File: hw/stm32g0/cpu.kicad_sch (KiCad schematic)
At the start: 32 parts, among them J201 Conn_01x06, J202 Conn_01x04, J203 Conn_01x03, U201 STM32G030K8Tx, U202 74AHCT125, U203 CAT24C256

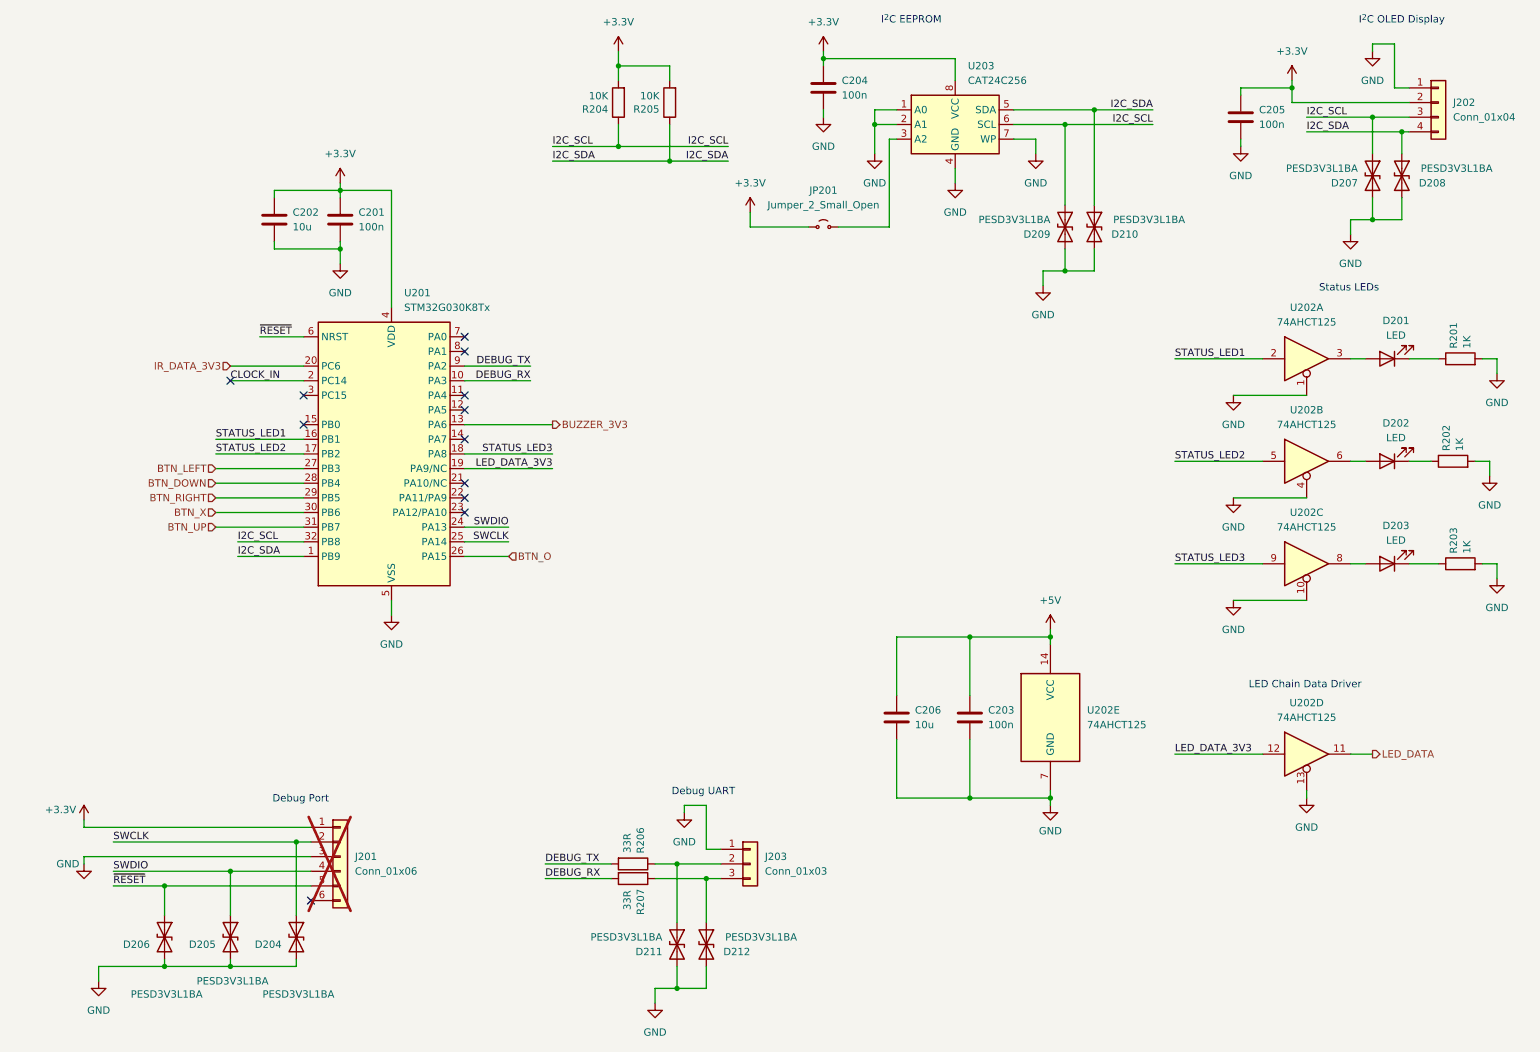
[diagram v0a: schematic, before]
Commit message: chore(hw): general improvements, utilize some unused CPU pins
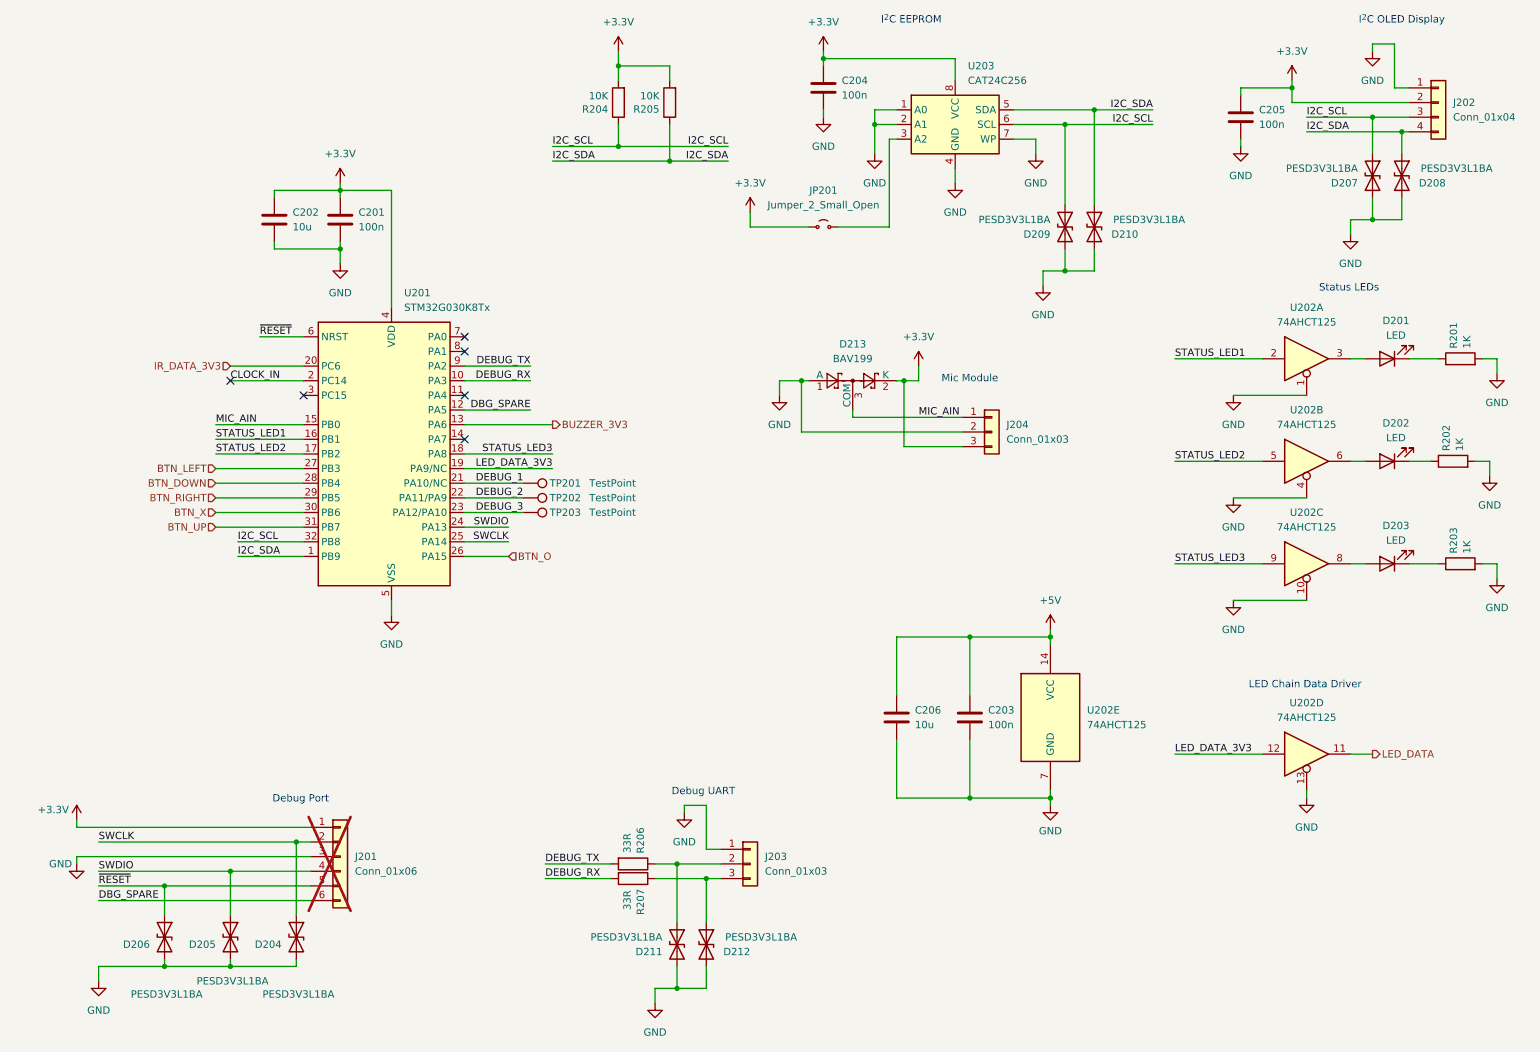
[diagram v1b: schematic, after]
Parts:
- added D213: BAV199, Package_TO_SOT_SMD:SOT-23_Handsoldering, symbol Diode:BAT54S
- added J204: Conn_01x03, Connector_PinHeader_2.54mm:PinHeader_1x03_P2.54mm_Vertical, symbol Connector_Generic:Conn_01x03
- added TP201, TP202, TP203: TestPoint, TestPoint:TestPoint_Pad_D1.0mm, symbol Connector:TestPoint
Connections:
- net +3.3V: now also D213.2 (K), J204.3 (Pin_3)
- net GND: now also D213.1 (A), J204.2 (Pin_2)
- net DBG_SPARE: now reaches U201.12 (PA5)
- net DBG_SPARE: now also J201.6 (Pin_6)
- net MIC_AIN: now reaches U201.15 (PB0)
- net MIC_AIN: now also D213.3 (COM), J204.1 (Pin_1)
- net DEBUG_1: now reaches U201.21 (PA10/NC)
- net DEBUG_1: now also TP201.1
- net DEBUG_2: now reaches U201.22 (PA11/PA9)
- net DEBUG_2: now also TP202.1
- net DEBUG_3: now reaches U201.23 (PA12/PA10)
- net DEBUG_3: now also TP203.1
- no-connect marks 12 -> 6
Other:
- note added: "Mic Module"

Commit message: chore(hw): move all signals to outer layers
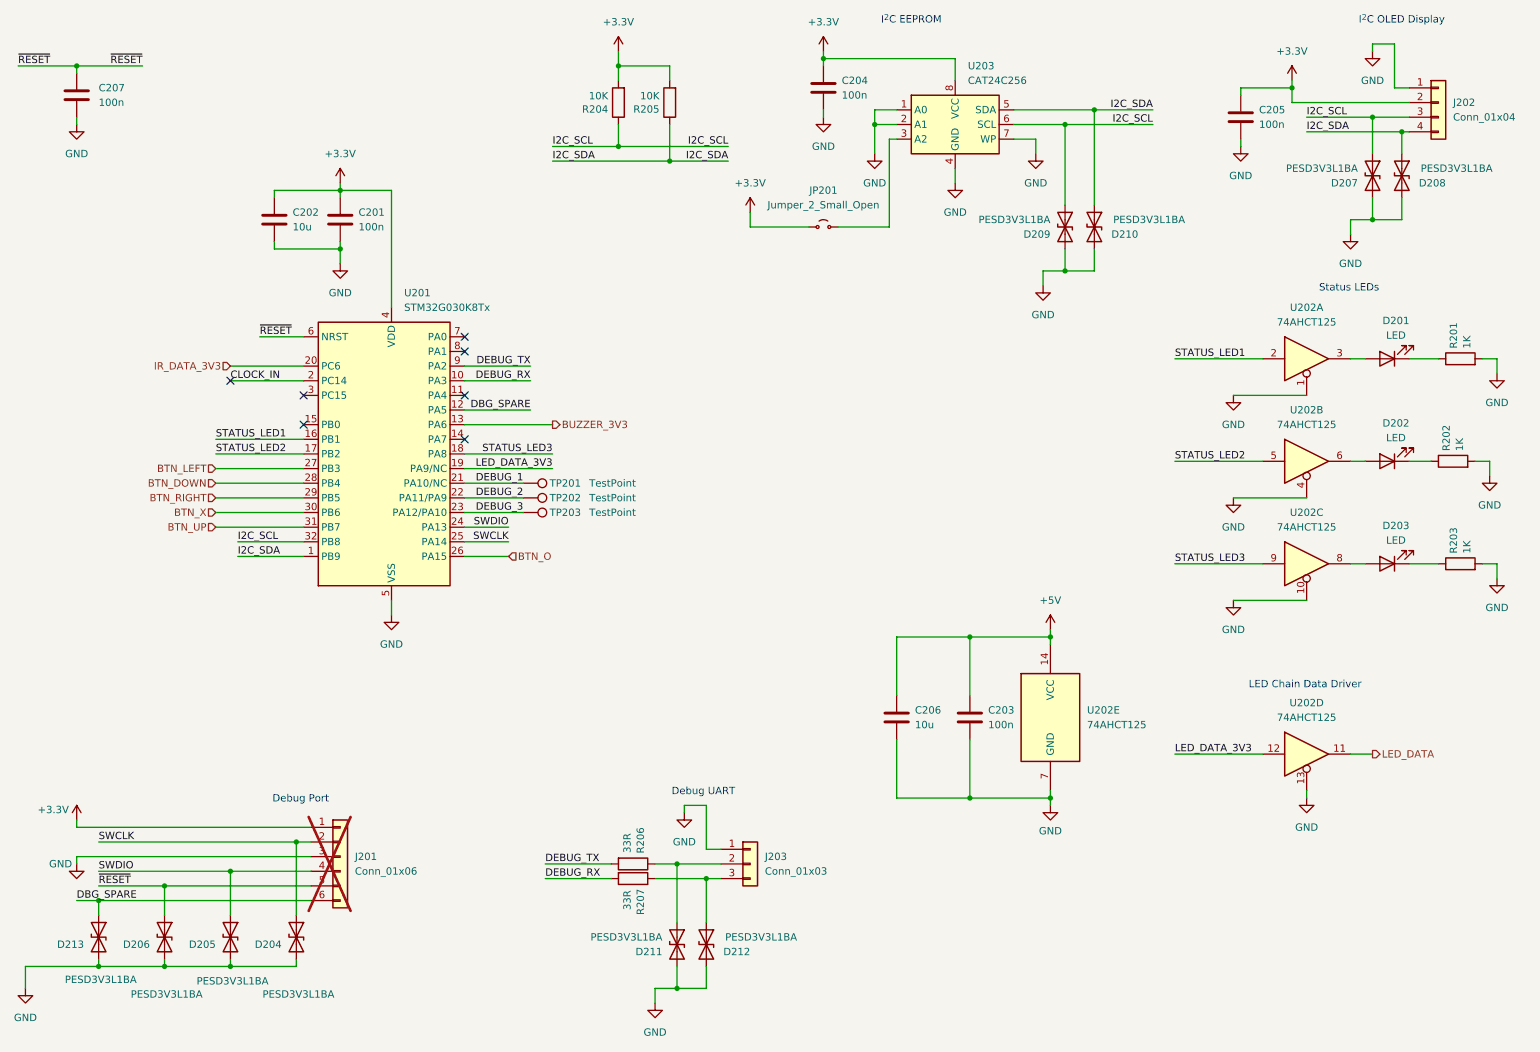
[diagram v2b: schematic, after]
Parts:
- removed D213: BAV199, Package_TO_SOT_SMD:SOT-23_Handsoldering, symbol Diode:BAT54S
- removed J204: Conn_01x03, Connector_PinHeader_2.54mm:PinHeader_1x03_P2.54mm_Vertical, symbol Connector_Generic:Conn_01x03
- added C207: 100n, Capacitor_SMD:C_0805_2012Metric_Pad1.18x1.45mm_HandSolder, symbol Device:C
- added D213: PESD3V3L1BA, Diode_SMD:D_SOD-323_HandSoldering, symbol Device:D_TVS
- TP201, TP202, TP203: footprint TestPoint:TestPoint_Pad_D1.0mm -> TestPoint:TestPoint_Pad_1.0x1.0mm
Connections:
- net DBG_SPARE: now also D213.1 (A1)
- net GND: now also C207.2, D213.2 (A2)
- net ~{RESET}: now also C207.1
- net MIC_AIN: no longer names the net of U201.15 (PB0)
- no-connect marks 6 -> 7
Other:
- note removed: "Mic Module"

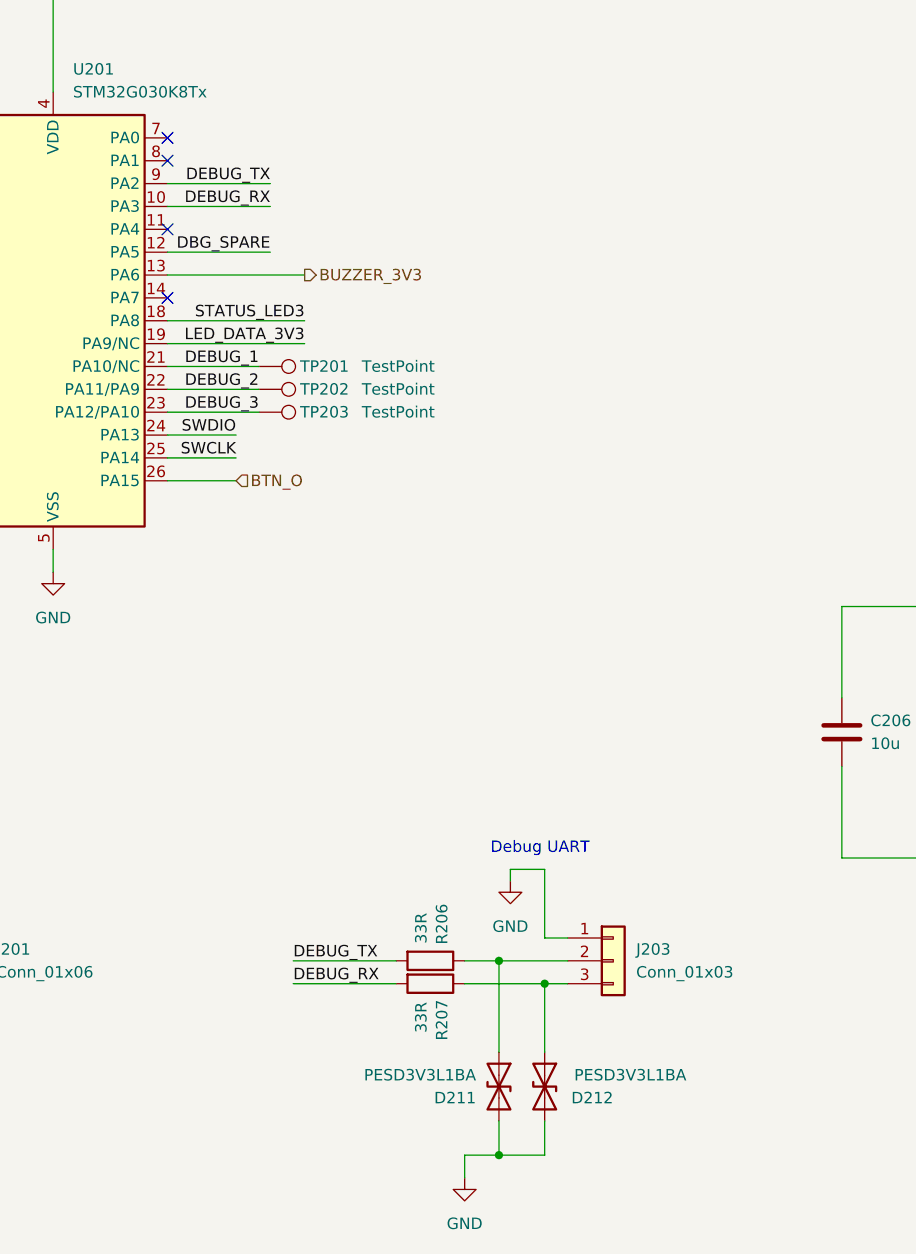
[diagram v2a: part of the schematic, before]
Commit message: chore(hw): add BT module supply and control pins
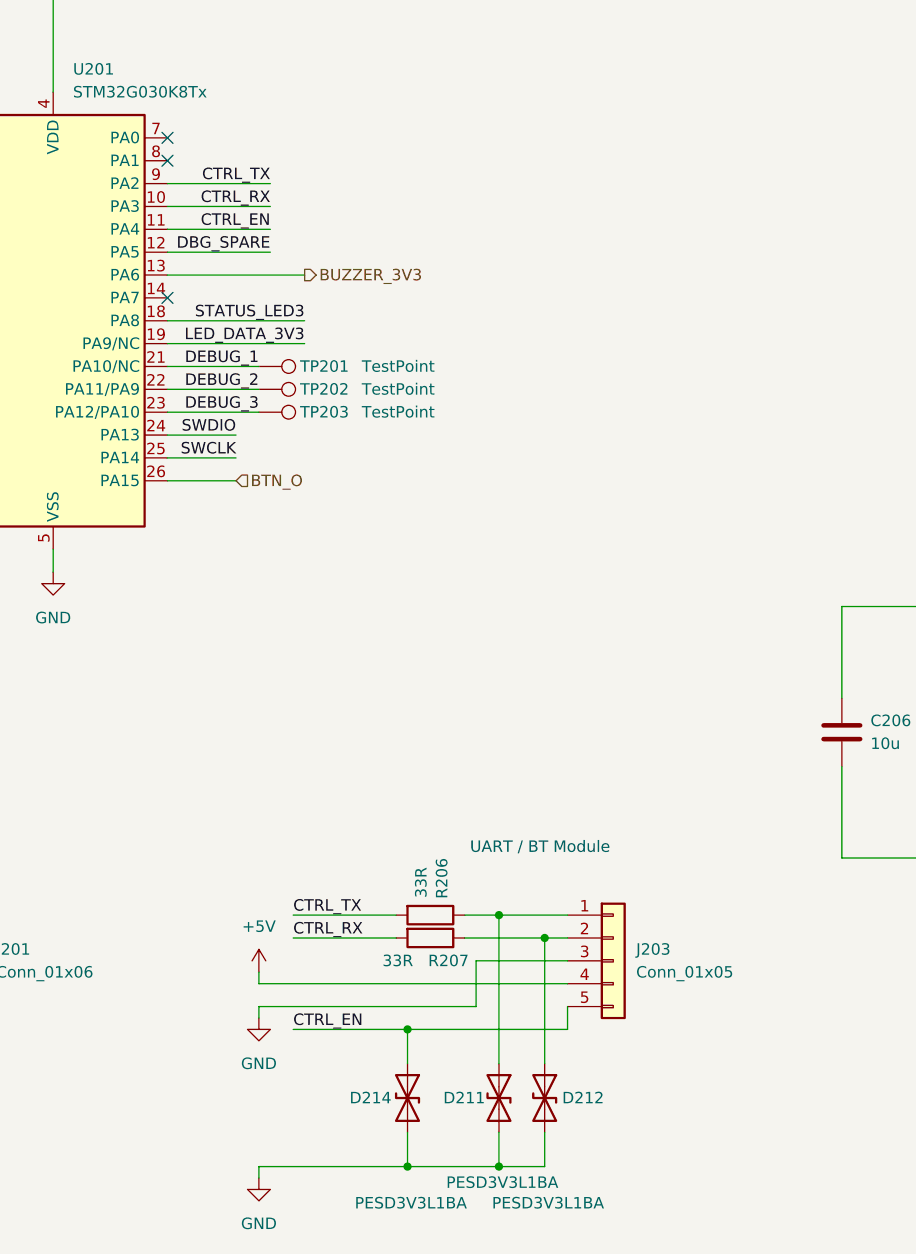
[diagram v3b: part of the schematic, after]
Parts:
- removed J203: Conn_01x03, Connector_PinHeader_2.54mm:PinHeader_1x03_P2.54mm_Vertical, symbol Connector_Generic:Conn_01x03
- added D214: PESD3V3L1BA, Diode_SMD:D_SOD-323_HandSoldering, symbol Device:D_TVS
- added J203: Conn_01x05, Connector_PinSocket_2.54mm:PinSocket_1x05_P2.54mm_Vertical, symbol Connector_Generic:Conn_01x05
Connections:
- net +5V: now also J203.4 (Pin_4)
- net GND: now also D214.2 (A2), J203.3 (Pin_3)
- net CTRL_EN: now reaches U201.11 (PA4)
- net CTRL_EN: now also D214.1 (A1), J203.5 (Pin_5)
- net at D212.1 (A1), R207.1: now also J203.2 (Pin_2)
- net at D211.1 (A1), R206.1: now also J203.1 (Pin_1)
- net DEBUG_RX renamed CTRL_RX
- net DEBUG_TX renamed CTRL_TX
- no-connect marks 7 -> 6
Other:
- note added: "UART / BT Module"
- note removed: "Debug UART"
- moved on the sheet: D211, D212, R206, R207

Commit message: chore(hw): change debug port to pin header
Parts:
- J201: footprint Connector_PinSocket_2.54mm:PinSocket_1x06_P2.54mm_Vertical -> Connector_PinHeader_2.54mm:PinHeader_1x06_P2.54mm_Vertical
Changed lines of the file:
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@@
 			)
 		)
-		(property "Footprint" "Connector_PinSocket_2.54mm:PinSocket_1x06_P2.54mm_Vertical"
+		(property "Footprint" "Connector_PinHeader_2.54mm:PinHeader_1x06_P2.54mm_Vertical"
 			(at 76.2 163.83 0)
 			(effects

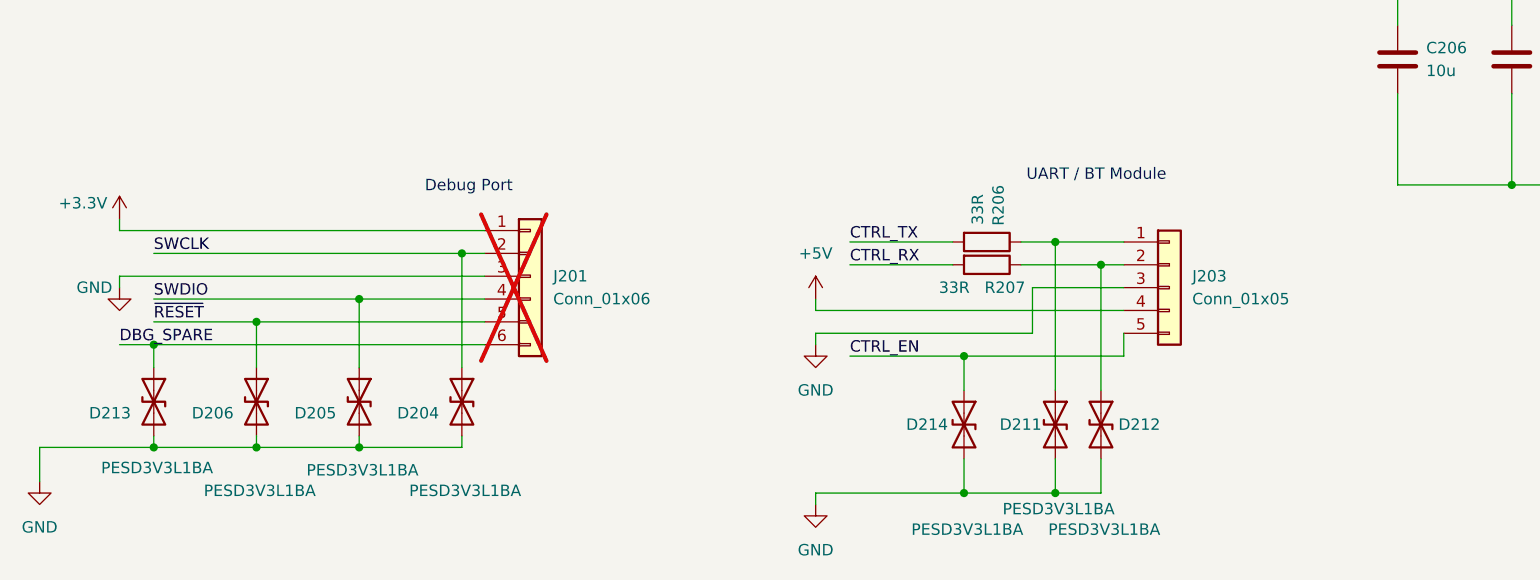
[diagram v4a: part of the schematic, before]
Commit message: chore(hw): add debug port resistors
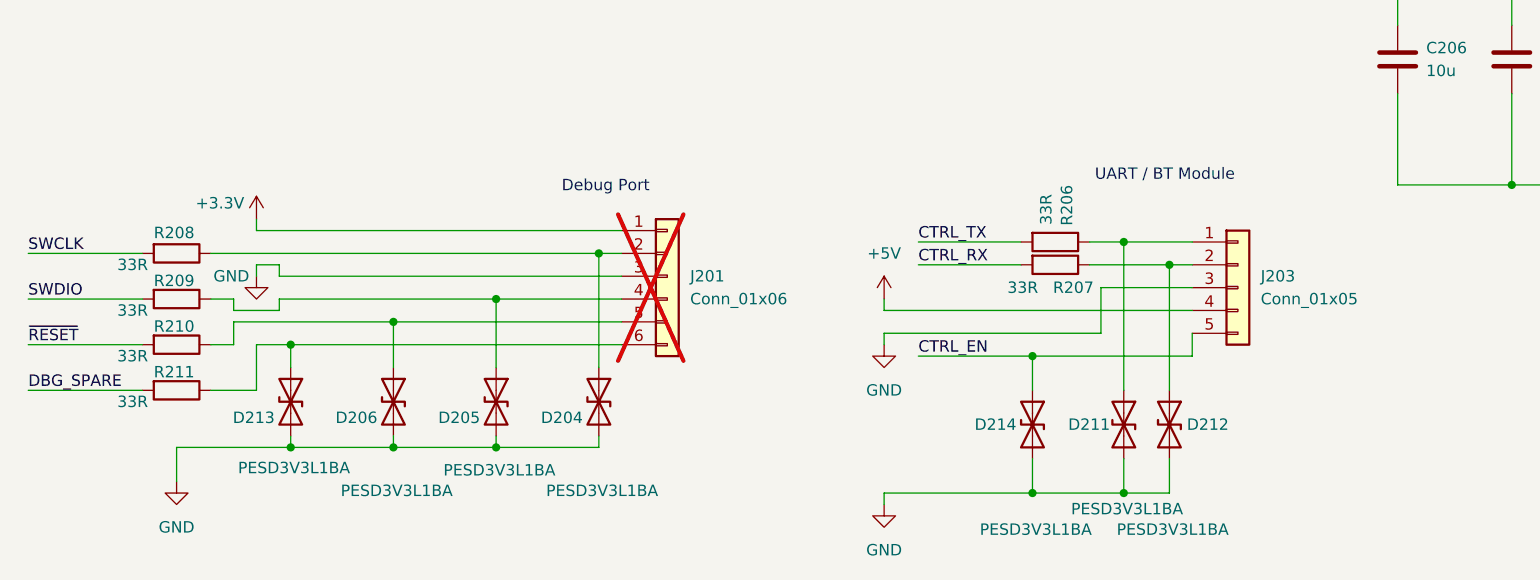
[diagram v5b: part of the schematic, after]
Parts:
- added R208, R209, R210, R211: 33R, Resistor_SMD:R_0805_2012Metric_Pad1.20x1.40mm_HandSolder, symbol Device:R
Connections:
- net DBG_SPARE: now also R211.2; no longer D213.1 (A1), J201.6 (Pin_6)
- net SWCLK: now also R208.2; no longer D204.1 (A1), J201.2 (Pin_2)
- net SWDIO: now also R209.2; no longer D205.1 (A1), J201.4 (Pin_4)
- net ~{RESET}: now also R210.2; no longer D206.1 (A1), J201.5 (Pin_5)
- new net: D204.1 (A1), J201.2 (Pin_2), R208.1
- new net: D213.1 (A1), J201.6 (Pin_6), R211.1
- new net: D205.1 (A1), J201.4 (Pin_4), R209.1
- new net: D206.1 (A1), J201.5 (Pin_5), R210.1
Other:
- moved on the sheet: D204, D205, D206, D211, D212, D213, D214, J201, J203, R206, R207
